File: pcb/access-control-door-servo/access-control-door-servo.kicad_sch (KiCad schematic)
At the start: 16 parts, among them J1 Conn_01x02_Pin, U1 ATtiny404-SS

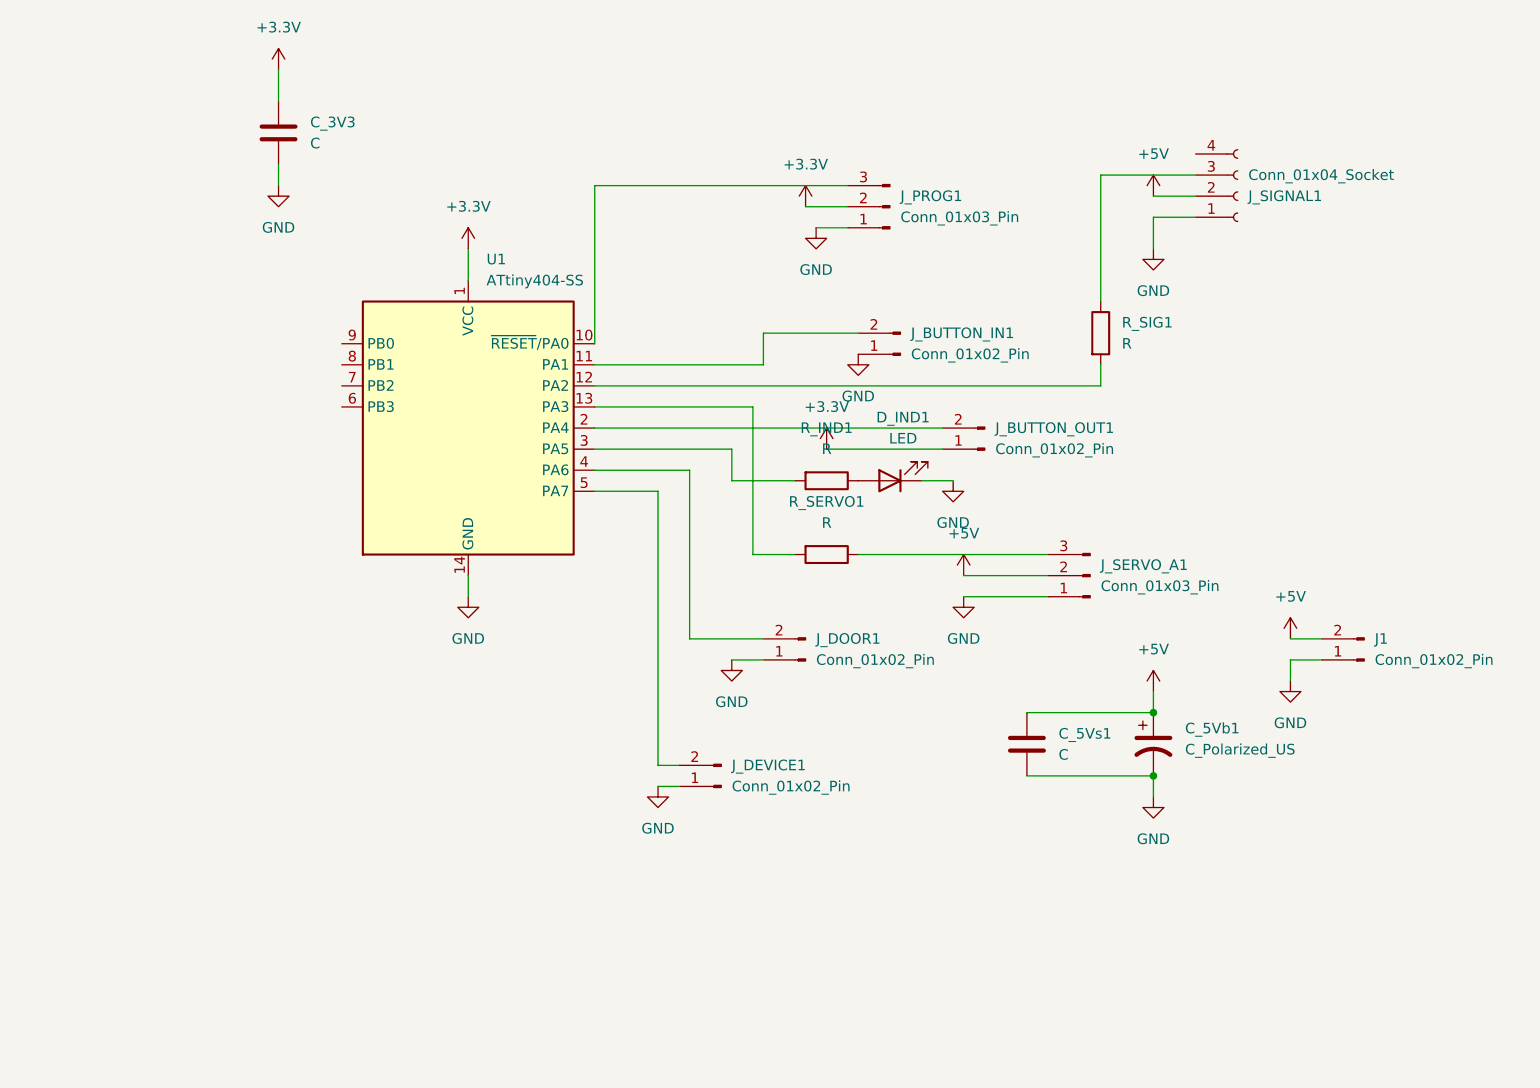
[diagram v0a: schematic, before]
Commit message: Progress with work to support door servo
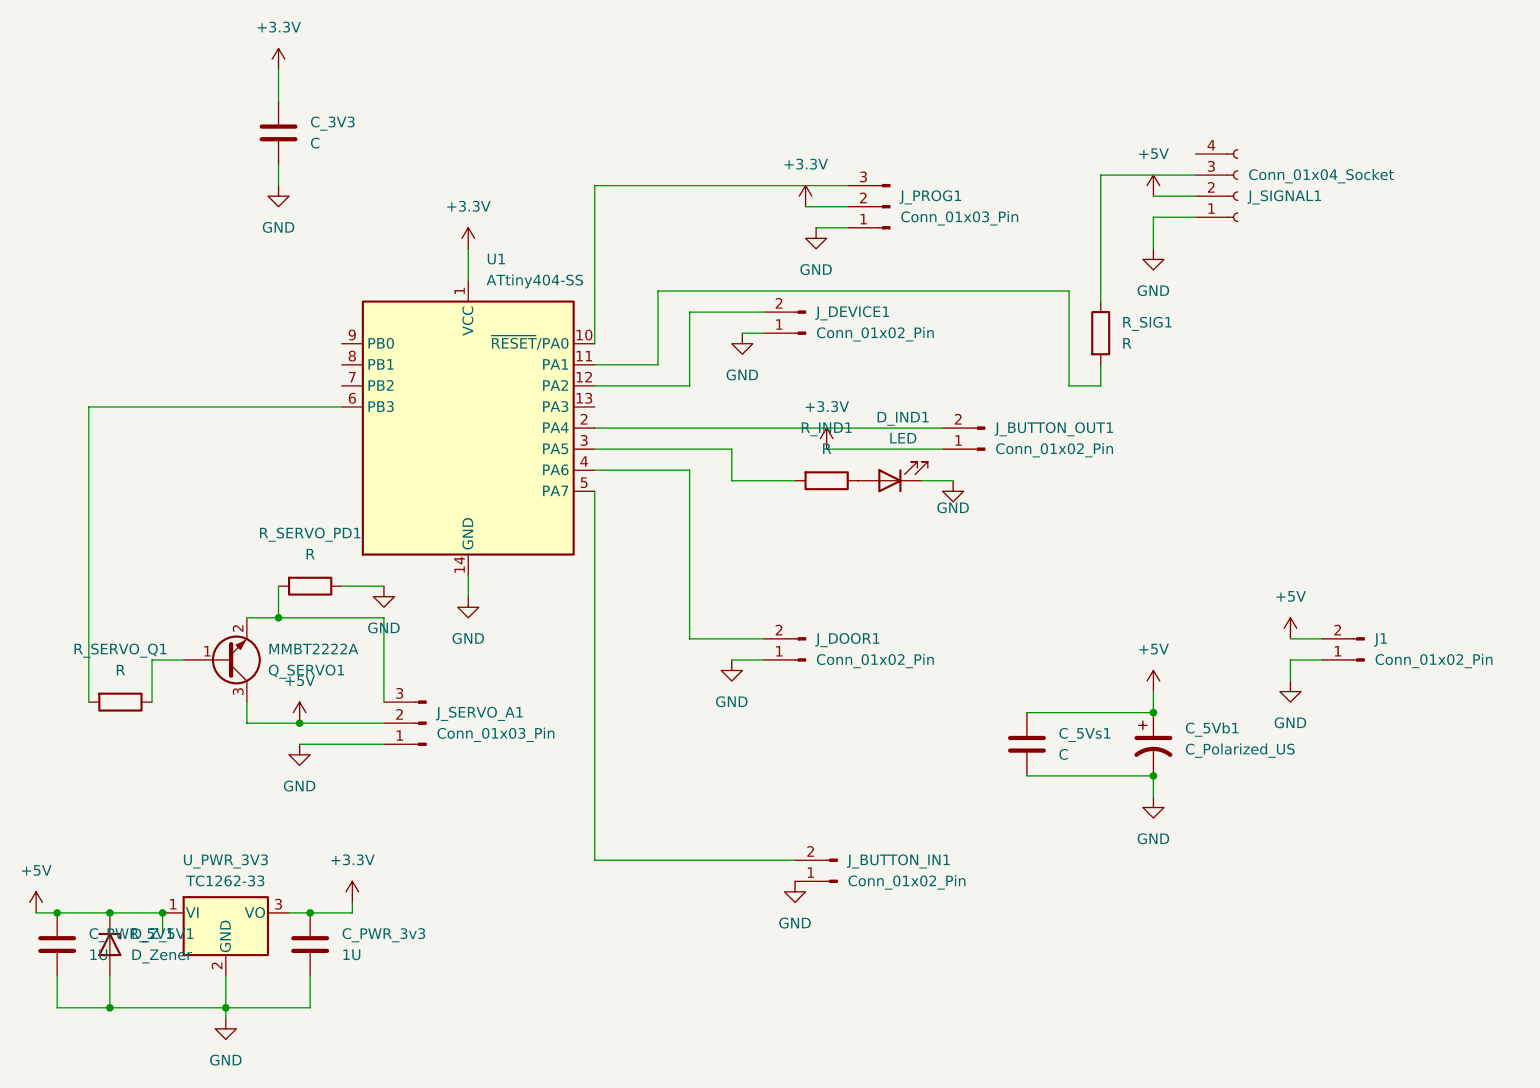
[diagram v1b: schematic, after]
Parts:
- added C_PWR_3v3, C_PWR_5V1: 1U, Capacitor_SMD:C_1206_3216Metric_Pad1.33x1.80mm_HandSolder, symbol Device:C
- added D_Z_5V1: D_Zener, Diode_SMD:D_1206_3216Metric_Pad1.42x1.75mm_HandSolder, symbol Device:D_Zener
- added Q_SERVO1: MMBT2222A, Package_TO_SOT_SMD:SOT-23W_Handsoldering, symbol Transistor_BJT:MMBT2222A
- added R_SERVO_PD1: R, Resistor_SMD:R_1206_3216Metric, symbol Device:R
- added U_PWR_3V3: TC1262-33, Package_TO_SOT_SMD:SOT-223-3_TabPin2, symbol Regulator_Linear:TC1262-33
- renumbered R_SERVO1 to R_SERVO_Q1
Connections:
- net +3.3V: now also C_PWR_3v3.1, U_PWR_3V3.3 (VO)
- net +5V: now also C_PWR_5V1.1, D_Z_5V1.1 (K), Q_SERVO1.3 (C), U_PWR_3V3.1 (VI)
- net GND: now also C_PWR_3v3.2, C_PWR_5V1.2, D_Z_5V1.2 (A), R_SERVO_PD1.1, U_PWR_3V3.2 (GND)
- net at R_SIG1.2: now also U1.11 (PA1); no longer U1.12 (PA2)
- net at J_SERVO_A1.3 (Pin_3): now also Q_SERVO1.2 (E), R_SERVO_PD1.2; no longer R_SERVO_Q1.1
- net at R_SERVO_Q1.2: now also U1.6 (PB3); no longer U1.13 (PA3)
- net at J_BUTTON_IN1.2 (Pin_2): now also U1.5 (PA7); no longer U1.11 (PA1)
- net at J_DEVICE1.2 (Pin_2): now also U1.12 (PA2); no longer U1.5 (PA7)
- new net: Q_SERVO1.1 (B), R_SERVO_Q1.1
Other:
- moved on the sheet: J_BUTTON_IN1, J_DEVICE1, J_SERVO_A1, R_SERVO_Q1

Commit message: Pads for TWI, space for 5v signal option
Copper on the back of relay
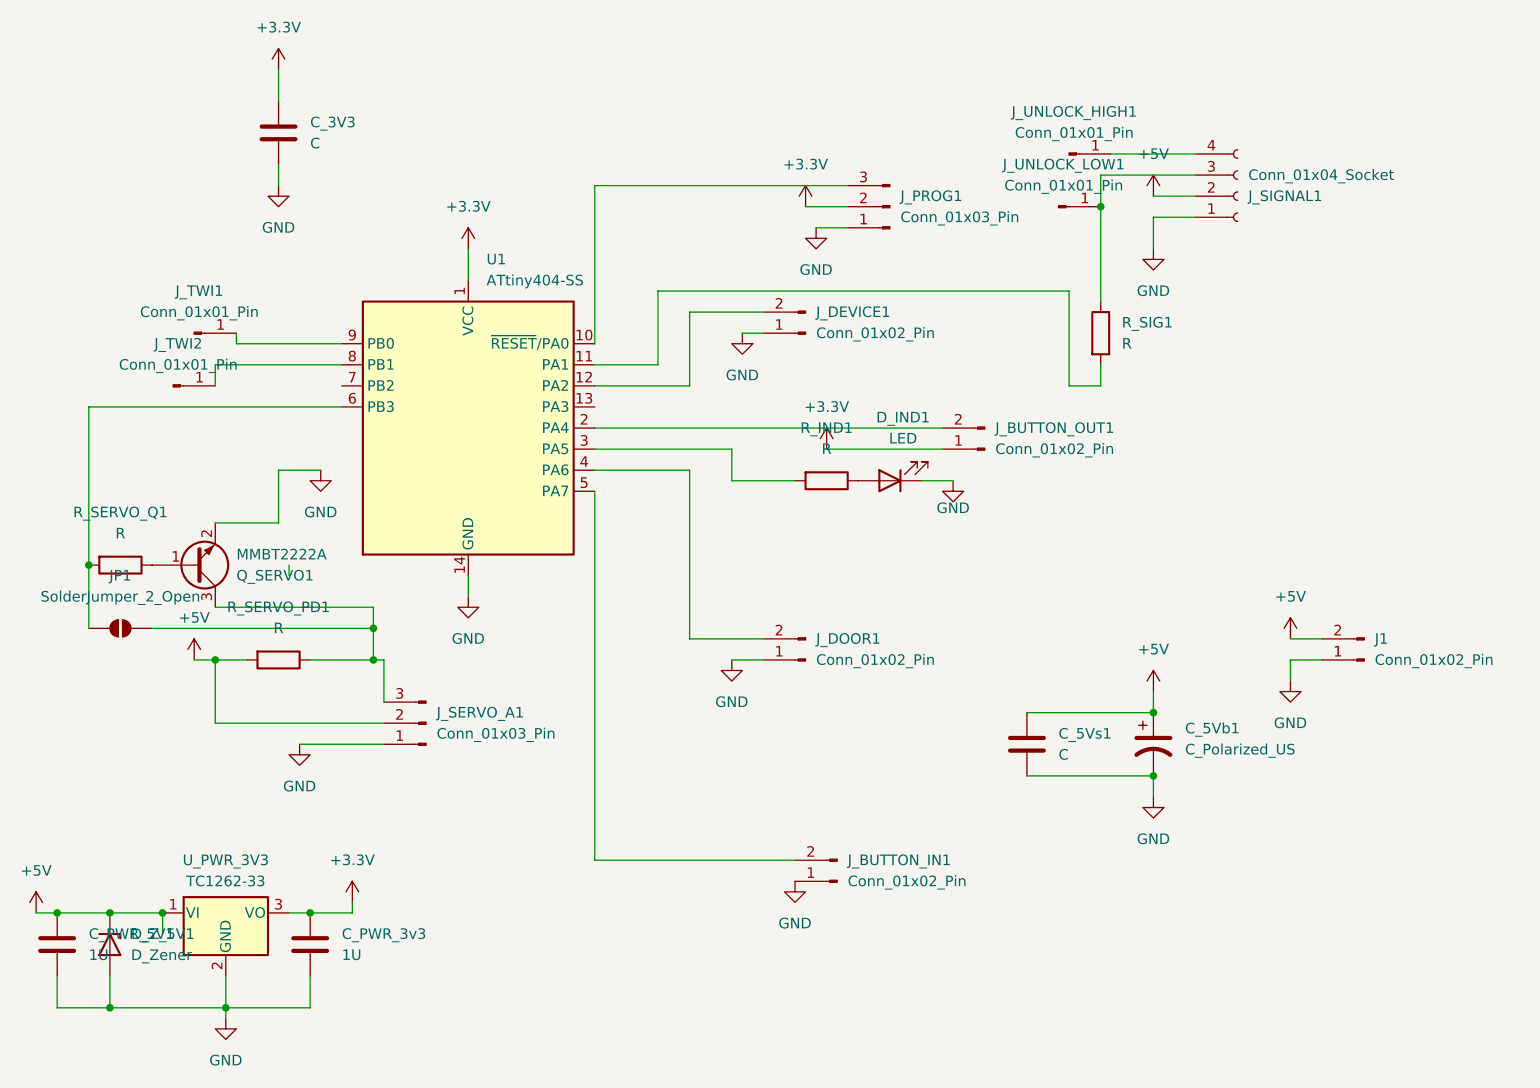
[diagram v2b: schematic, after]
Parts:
- added JP1: SolderJumper_2_Open, Jumper:SolderJumper-2_P1.3mm_Open_TrianglePad1.0x1.5mm, symbol Jumper:SolderJumper_2_Open
- added J_TWI1, J_TWI2, J_UNLOCK_HIGH1, J_UNLOCK_LOW1: Conn_01x01_Pin, Connector_Wire:SolderWirePad_1x01_SMD_1x2mm, symbol Connector:Conn_01x01_Pin
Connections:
- net +5V: now also R_SERVO_PD1.2; no longer Q_SERVO1.3 (C)
- net GND: now also Q_SERVO1.2 (E); no longer R_SERVO_PD1.1
- net at J_SIGNAL1.3 (Pin_3), R_SIG1.1: now also J_UNLOCK_LOW1.1 (Pin_1)
- net at R_SERVO_Q1.2, U1.6 (PB3): now also JP1.1 (A)
- net at J_SIGNAL1.4 (Pin_4): now also J_UNLOCK_HIGH1.1 (Pin_1)
- net at U1.8 (PB1): now also J_TWI2.1 (Pin_1)
- net at U1.9 (PB0): now also J_TWI1.1 (Pin_1)
- new net: JP1.2 (B), J_SERVO_A1.3 (Pin_3), Q_SERVO1.3 (C), R_SERVO_PD1.1
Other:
- moved on the sheet: Q_SERVO1, R_SERVO_PD1, R_SERVO_Q1

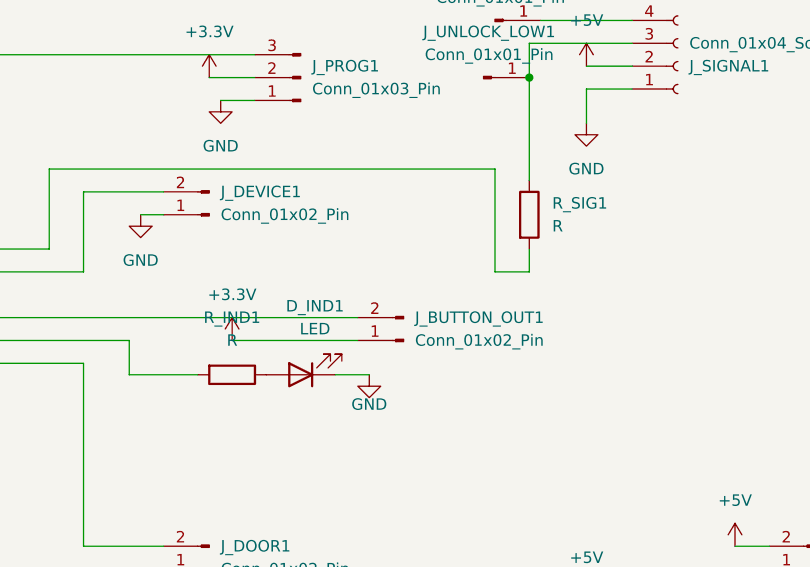
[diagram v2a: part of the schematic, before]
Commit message: Correct compontent value for Tim
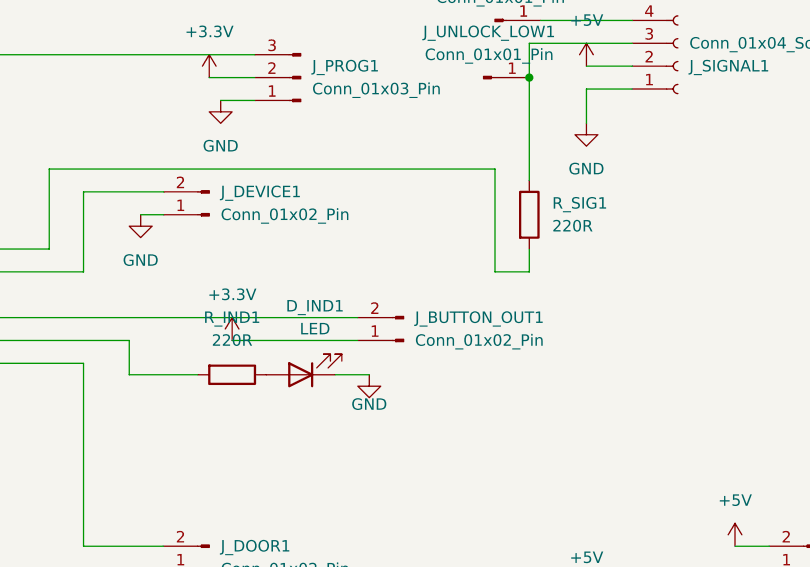
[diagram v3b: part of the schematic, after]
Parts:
- R_IND1, R_SIG1: value R -> 220R
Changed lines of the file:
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@@
 			)
 		)
-		(property "Value" "R"
+		(property "Value" "220R"
 			(at 177.8 93.98 90)
 			(effects
@@
 			)
 		)
-		(property "Value" "R"
+		(property "Value" "220R"
 			(at 213.36 81.2799 0)
 			(effects
